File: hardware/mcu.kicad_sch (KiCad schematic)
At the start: 21 parts, among them J201 STDC14

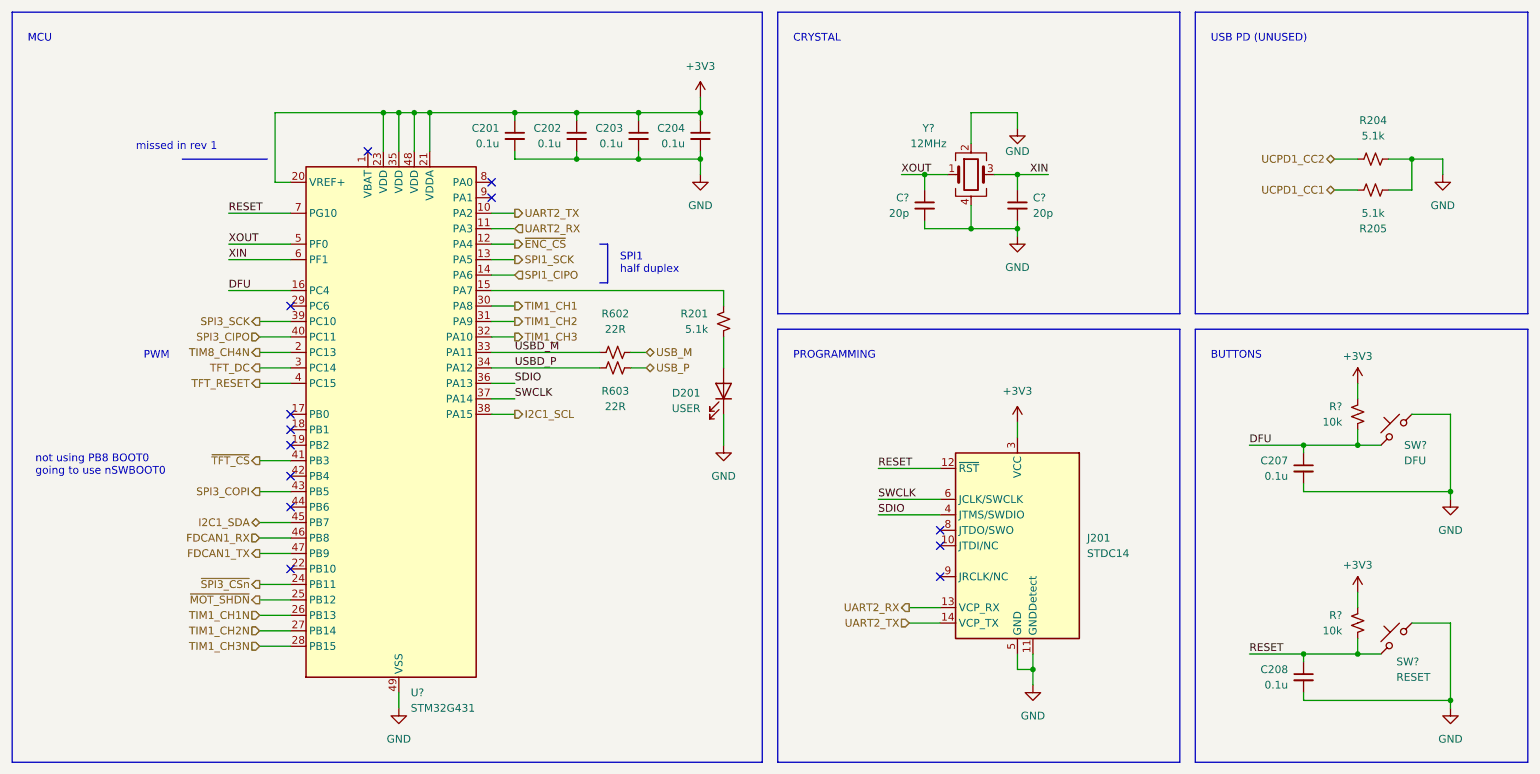
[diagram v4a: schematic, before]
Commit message: get USB detection working
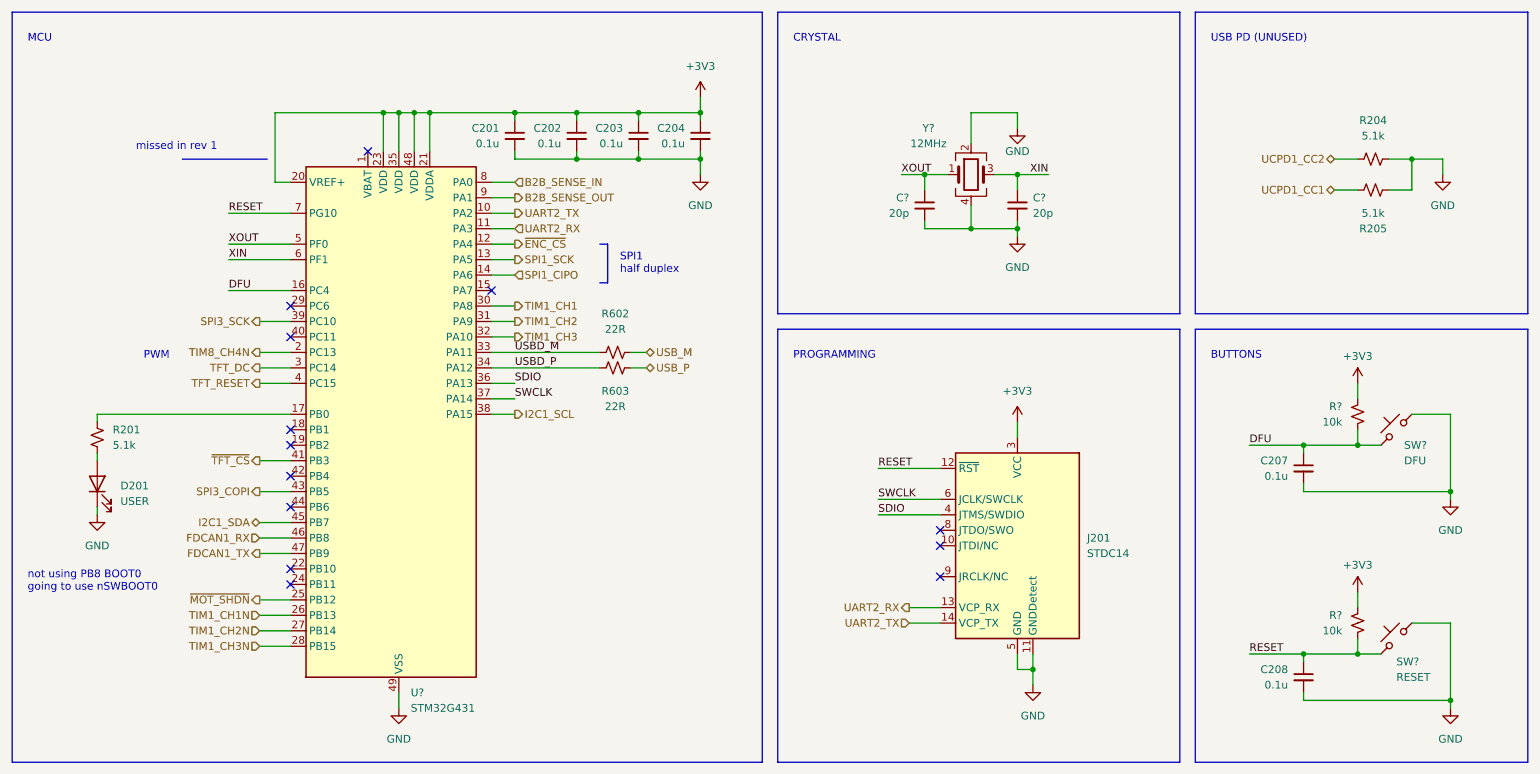
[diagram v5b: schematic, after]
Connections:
- net at R201.1: now also U?.17 (PB0); no longer U?.15 (PA7)
- net B2B_SENSE_IN: now reaches U?.8 (PA0)
- net B2B_SENSE_OUT: now reaches U?.9 (PA1)
- net SPI3_CIPO: no longer names the net of U?.40 (PC11)
- net ~{SPI3_CSn}: no longer names the net of U?.24 (PB11)
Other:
- moved on the sheet: D201, R201
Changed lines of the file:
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@@
   (junction (at 181.61 57.15) (diameter 0) (color 0 0 0 0)
   )
+  (no_connect (at 69.85 115.57))
+  (no_connect (at 69.85 74.93))
   (no_connect (at 69.85 102.87))
   (no_connect (at 176.53 106.68))
@@
   (no_connect (at 69.85 97.79))
   (no_connect (at 176.53 114.3))
-  (no_connect (at 102.87 49.53))
+  (no_connect (at 102.87 67.31))
   (no_connect (at 69.85 69.85))
   (no_connect (at 82.55 44.45))
-  (no_connect (at 102.87 52.07))
-  (no_connect (at 69.85 87.63))
   (no_connect (at 69.85 113.03))
   (no_connect (at 176.53 109.22))
@@
     (stroke (width 0) (type default))
   )
+  (wire (pts (xy 102.87 52.07) (xy 106.68 52.07))
+    (stroke (width 0) (type default))
+  )
+  (wire (pts (xy 102.87 49.53) (xy 106.68 49.53))
+    (stroke (width 0) (type default))
+  )
   (wire (pts (xy 87.63 38.1) (xy 87.63 44.45))
     (stroke (width 0) (type default))
@@
     (stroke (width 0) (type default))
   )
-  (wire (pts (xy 64.77 74.93) (xy 69.85 74.93))
-    (stroke (width 0) (type default))
-  )
   (wire (pts (xy 64.77 107.95) (xy 69.85 107.95))
     (stroke (width 0) (type default))
@@
     (stroke (width 0) (type default))
   )
-  (wire (pts (xy 102.87 67.31) (xy 140.97 67.31))
-    (stroke (width 0) (type default))
-  )
-  (wire (pts (xy 140.97 74.93) (xy 140.97 80.01))
+  (wire (pts (xy 38.1 93.98) (xy 38.1 95.25))
     (stroke (width 0) (type default))
   )
@@
     (stroke (width 0) (type default))
   )
-  (wire (pts (xy 140.97 67.31) (xy 140.97 69.85))
+  (wire (pts (xy 38.1 87.63) (xy 38.1 88.9))
     (stroke (width 0) (type default))
   )
@@
     (stroke (width 0) (type default))
   )
-  (wire (pts (xy 140.97 87.63) (xy 140.97 92.71))
+  (wire (pts (xy 38.1 102.87) (xy 38.1 104.14))
     (stroke (width 0) (type default))
   )
@@
     (stroke (width 0) (type default))
   )
+  (wire (pts (xy 38.1 87.63) (xy 69.85 87.63))
+    (stroke (width 0) (type default))
+  )
   (wire (pts (xy 245.11 92.71) (xy 248.92 92.71))
     (stroke (width 0) (type default))
@@
     (stroke (width 0) (type default))
   )
-  (wire (pts (xy 64.77 115.57) (xy 69.85 115.57))
-    (stroke (width 0) (type default))
-  )
   (polyline (pts (xy 218.44 71.12) (xy 273.05 71.12))
     (stroke (width 0) (type default))
@@
     (effects (font (size 1.27 1.27)) (justify left bottom))
   )
-  (text "not using PB8 BOOT0\ngoing to use nSWBOOT0" (at 27.94 97.79 0)
+  (text "not using PB8 BOOT0\ngoing to use nSWBOOT0" (at 26.67 116.84 0)
     (effects (font (size 1.27 1.27)) (justify left bottom))
   )
@@
     (effects (font (size 1.27 1.27)) (justify right))
   )
+  (hierarchical_label "B2B_SENSE_IN" (shape input) (at 106.68 49.53 0) (fields_autoplaced)
+    (effects (font (size 1.27 1.27)) (justify left))
+  )
   (hierarchical_label "SPI3_COPI" (shape output) (at 64.77 100.33 180) (fields_autoplaced)
     (effects (font (size 1.27 1.27)) (justify right))
   )
   (hierarchical_label "TFT_DC" (shape output) (at 64.77 80.01 180) (fields_autoplaced)
-    (effects (font (size 1.27 1.27)) (justify right))
-  )
-  (hierarchical_label "~{SPI3_CSn}" (shape output) (at 64.77 115.57 180) (fields_autoplaced)
     (effects (font (size 1.27 1.27)) (justify right))
   )
@@
     (effects (font (size 1.27 1.27)) (justify left))
   )
-  (hierarchical_label "SPI3_CIPO" (shape input) (at 64.77 74.93 180) (fields_autoplaced)
-    (effects (font (size 1.27 1.27)) (justify right))
-  )
   (hierarchical_label "FDCAN1_TX" (shape output) (at 64.77 110.49 180) (fields_autoplaced)
     (effects (font (size 1.27 1.27)) (justify right))
@@
   (hierarchical_label "UART2_RX" (shape output) (at 171.45 119.38 180) (fields_autoplaced)
     (effects (font (size 1.27 1.27)) (justify right))
+  )
+  (hierarchical_label "B2B_SENSE_OUT" (shape output) (at 106.68 52.07 0) (fields_autoplaced)
+    (effects (font (size 1.27 1.27)) (justify left))
   )
   (hierarchical_label "~{TFT_CS}" (shape output) (at 64.77 95.25 180) (fields_autoplaced)
@@
     )
   )
-  (symbol (lib_id "Device:R_Small_US") (at 140.97 72.39 0) (mirror y) (unit 1)
+  (symbol (lib_id "Device:R_Small_US") (at 38.1 91.44 0) (unit 1)
     (in_bom yes) (on_board yes) (dnp no)
-    (property "Reference" "R201" (at 138.43 71.12 0)
-      (effects (font (size 1.27 1.27)) (justify left))
-    )
-    (property "Value" "5.1k" (at 138.43 73.66 0)
-      (effects (font (size 1.27 1.27)) (justify left))
-    )
-    (property "Footprint" "Resistor_SMD:R_0402_1005Metric" (at 140.97 72.39 0)
-      (effects (font (size 1.27 1.27)) hide)
-    )
-    (property "Datasheet" "~" (at 140.97 72.39 0)
+    (property "Reference" "R201" (at 40.64 90.17 0)
+      (effects (font (size 1.27 1.27)) (justify left))
+    )
+    (property "Value" "5.1k" (at 40.64 92.71 0)
+      (effects (font (size 1.27 1.27)) (justify left))
+    )
+    (property "Footprint" "Resistor_SMD:R_0402_1005Metric" (at 38.1 91.44 0)
+      (effects (font (size 1.27 1.27)) hide)
+    )
+    (property "Datasheet" "~" (at 38.1 91.44 0)
       (effects (font (size 1.27 1.27)) hide)
     )
@@
     )
   )
-  (symbol (lib_id "Device:LED") (at 140.97 83.82 270) (mirror x) (unit 1)
-    (in_bom yes) (on_board yes) (dnp no) (fields_autoplaced)
-    (property "Reference" "D201" (at 137.16 84.1375 90)
+  (symbol (lib_id "Device:LED") (at 38.1 99.06 90) (unit 1)
+    (in_bom yes) (on_board yes) (dnp no) (fields_autoplaced)
+    (property "Reference" "D201" (at 41.91 99.3775 90)
       (effects (font (size 1.27 1.27)) (justify right))
     )
-    (property "Value" "USER" (at 137.16 86.6775 90)
+    (property "Value" "USER" (at 41.91 101.9175 90)
       (effects (font (size 1.27 1.27)) (justify right))
     )
-    (property "Footprint" "Diode_SMD:D_0603_1608Metric" (at 140.97 83.82 0)
-      (effects (font (size 1.27 1.27)) hide)
-    )
-    (property "Datasheet" "~" (at 140.97 83.82 0)
+    (property "Footprint" "Diode_SMD:D_0603_1608Metric" (at 38.1 99.06 0)
+      (effects (font (size 1.27 1.27)) hide)
+    )
+    (property "Datasheet" "~" (at 38.1 99.06 0)
       (effects (font (size 1.27 1.27)) hide)
     )
@@
     )
   )
-  (symbol (lib_id "power:GND") (at 140.97 92.71 0) (mirror y) (unit 1)
-    (in_bom yes) (on_board yes) (dnp no) (fields_autoplaced)
-    (property "Reference" "#PWR0111" (at 140.97 99.06 0)
-      (effects (font (size 1.27 1.27)) hide)
-    )
-    (property "Value" "GND" (at 140.97 97.79 0)
-      (effects (font (size 1.27 1.27)))
-    )
-    (property "Footprint" "" (at 140.97 92.71 0)
-      (effects (font (size 1.27 1.27)) hide)
-    )
-    (property "Datasheet" "" (at 140.97 92.71 0)
-      (effects (font (size 1.27 1.27)) hide)
-    )
+  (symbol (lib_id "power:GND") (at 38.1 104.14 0) (unit 1)
+    (in_bom yes) (on_board yes) (dnp no) (fields_autoplaced)
+    (property "Reference" "#PWR0111" (at 38.1 110.49 0)
+      (effects (font (size 1.27 1.27)) hide)
+    )
+    (property "Value" "GND" (at 38.1 109.22 0)
+      (effects (font (size 1.27 1.27)))
+    )
+    (property "Footprint" "" (at 38.1 104.14 0)
+      (effects (font (size 1.27 1.27)) hide)
+    )
+    (property "Datasheet" "" (at 38.1 104.14 0)
+      (effects (font (size 1.27 1.27)) hide)
+    )
